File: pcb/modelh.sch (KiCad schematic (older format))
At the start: 39 parts, among them J1 USB_B, J2 Conn_01x16, J3 Conn_01x08, J4 Conn_01x04, J5 Conn_02x03_Odd_Even, J6 Conn_02x05_Odd_Even, SW1 SW_Push, U1 STM32F103C8Tx, U2 AMS1117-3.3, Y1 8MHz, Y2 32.768KHz

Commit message: Fix DRC
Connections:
- no-connect marks 2 -> 3
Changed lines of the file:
@@
 	1    0    0    -1
 $EndComp
-Text HLabel 9800 1950 0    50   Input ~ 0
-col7
-Text HLabel 9800 1850 0    50   Input ~ 0
-col6
-Text HLabel 9800 1750 0    50   Input ~ 0
-col5
-Text HLabel 9800 1650 0    50   Input ~ 0
-col4
-Text HLabel 9800 1550 0    50   Input ~ 0
-col3
-Text HLabel 9800 1450 0    50   Input ~ 0
-col2
-Text HLabel 9800 1350 0    50   Input ~ 0
-col1
-Text HLabel 9800 1250 0    50   Input ~ 0
-col0
 Wire Wire Line
 	10100 1250 9800 1250
@@
 Wire Wire Line
 	9800 1950 10100 1950
-Text HLabel 9800 2450 0    50   Input ~ 0
-col12
-Text HLabel 9800 2750 0    50   Input ~ 0
-col15
-Text HLabel 9800 2650 0    50   Input ~ 0
-col14
-Text HLabel 9800 2550 0    50   Input ~ 0
-col13
-Text HLabel 9800 2350 0    50   Input ~ 0
-col11
-Text HLabel 9800 2250 0    50   Input ~ 0
-col10
-Text HLabel 9800 2150 0    50   Input ~ 0
-col9
-Text HLabel 9800 2050 0    50   Input ~ 0
-col8
 Wire Wire Line
 	10100 2050 9800 2050
@@
 Wire Wire Line
 	9800 2750 10100 2750
-Text HLabel 9800 3900 0    50   Input ~ 0
-row7
-Text HLabel 9800 3800 0    50   Input ~ 0
-row6
-Text HLabel 9800 3700 0    50   Input ~ 0
-row5
-Text HLabel 9800 3600 0    50   Input ~ 0
-row4
-Text HLabel 9800 3500 0    50   Input ~ 0
-row3
-Text HLabel 9800 3400 0    50   Input ~ 0
-row2
-Text HLabel 9800 3300 0    50   Input ~ 0
-row1
-Text HLabel 9800 3200 0    50   Input ~ 0
-row0
 Wire Wire Line
 	10100 3200 9800 3200
@@
 	0    1    1    0
 $EndComp
-Text HLabel 9200 4750 0    50   Input ~ 0
-led2
-Text HLabel 9200 4550 0    50   Input ~ 0
-led1
-Text HLabel 9200 4450 0    50   Input ~ 0
-led0
 Wire Wire Line
 	9200 4450 9500 4450
@@
 Wire Wire Line
 	2250 1100 2250 1000
-Text HLabel 2350 1400 2    50   Input ~ 0
-D-
-Text HLabel 2350 1300 2    50   Input ~ 0
-D+
 $Comp
 L Device:R R3
@@
 	1    0    0    -1
 $EndComp
-Text HLabel 4800 4600 0    50   Input ~ 0
-col7
-Text HLabel 4800 4700 0    50   Input ~ 0
-col6
 Wire Wire Line
 	5100 4700 4800 4700
 Wire Wire Line
 	4800 4600 5100 4600
-Text HLabel 6700 4100 2    50   Input ~ 0
-col12
-Text HLabel 6700 3800 2    50   Input ~ 0
-col15
-Text HLabel 6700 3900 2    50   Input ~ 0
-col14
-Text HLabel 6700 4000 2    50   Input ~ 0
-col13
-Text HLabel 6700 4200 2    50   Input ~ 0
-col11
-Text HLabel 4800 3500 0    50   Input ~ 0
-col10
-Text HLabel 4800 3600 0    50   Input ~ 0
-col9
-Text HLabel 4800 4500 0    50   Input ~ 0
-col8
 Wire Wire Line
 	5100 4500 4800 4500
@@
 Wire Wire Line
 	6700 3800 6400 3800
-Text HLabel 4800 4100 0    50   Input ~ 0
-row0
 Wire Wire Line
 	5100 4100 4800 4100
-Text HLabel 4800 3300 0    50   Input ~ 0
-OSC32OUT
-Text HLabel 4800 3200 0    50   Input ~ 0
-OSC32IN
-Text HLabel 4800 2900 0    50   Input ~ 0
-OSC8OUT
-Text HLabel 4800 2800 0    50   Input ~ 0
-OSC8IN
 Wire Wire Line
 	5100 2800 4800 2800
@@
 Wire Wire Line
 	5100 2400 4800 2400
-Text HLabel 4150 6800 2    50   Input ~ 0
-nRST
 Wire Wire Line
 	4150 6800 3850 6800
@@
 	5550 7500 5650 7500
 Connection ~ 5650 7500
-Text HLabel 6300 6750 2    50   Input ~ 0
-OSC8OUT
-Text HLabel 6300 6450 2    50   Input ~ 0
-OSC8IN
 $Comp
 L Device:R R6
@@
 	6100 6750 5650 6750
 Connection ~ 5650 6750
-Text HLabel 6050 7500 2    50   Input ~ 0
-OSC32OUT
-Text HLabel 6050 7200 2    50   Input ~ 0
-OSC32IN
 Wire Wire Line
 	5650 7200 6050 7200
@@
 Wire Wire Line
 	5100 3900 4800 3900
-Text HLabel 4800 3900 0    50   Input ~ 0
-row2
-Text HLabel 6700 5000 2    50   Input ~ 0
-row3
-Text HLabel 4800 3800 0    50   Input ~ 0
-row4
 Wire Wire Line
 	6700 4900 6400 4900
 Wire Wire Line
 	6400 4800 6700 4800
-Text HLabel 6700 4800 2    50   Input ~ 0
-SWDIO
-Text HLabel 6700 4900 2    50   Input ~ 0
-SWCLK
 $Comp
 L power:GND #PWR0107
@@
 Wire Wire Line
 	1450 6450 1450 6350
-Text HLabel 4800 3100 0    50   Input ~ 0
-STATUSLED
 Wire Wire Line
 	5100 3100 4800 3100
-Text HLabel 1450 6350 1    50   Input ~ 0
-STATUSLED
 $Comp
 L power:+3.3V #PWR0108
@@
 	1    0    0    -1
 $EndComp
-Text HLabel 4800 2400 0    50   Input ~ 0
-nRST
 $Comp
 L Regulator_Linear:AMS1117-3.3 U2
@@
 Wire Wire Line
 	5100 2600 4800 2600
-Text HLabel 4800 2600 0    50   Input ~ 0
-BOOT0
 $Comp
 L power:GND #PWR0115
@@
 	5900 5300 5800 5300
 Connection ~ 5800 5300
-Text HLabel 6700 4600 2    50   Input ~ 0
-D-
-Text HLabel 6700 4700 2    50   Input ~ 0
-D+
 Wire Wire Line
 	6700 4600 6400 4600
@@
 Wire Wire Line
 	1550 5150 1250 5150
-Text HLabel 1250 5150 0    50   Input ~ 0
-BOOT0
 $Comp
 L power:+3.3V #PWR0116
@@
 Wire Wire Line
 	7700 1300 8000 1300
-Text HLabel 8000 1300 2    50   Input ~ 0
-SWDIO
-Text HLabel 8000 1400 2    50   Input ~ 0
-SWCLK
 Wire Wire Line
 	7700 1700 8000 1700
-Text HLabel 8000 1700 2    50   Input ~ 0
-nRST
 $Comp
 L Device:C C10
@@
 Wire Wire Line
 	6400 4500 6700 4500
-Text HLabel 6700 4500 2    50   Input ~ 0
-col0
-Text HLabel 6700 4400 2    50   Input ~ 0
-col1
-Text HLabel 6700 4300 2    50   Input ~ 0
-col2
-Text HLabel 4800 5000 0    50   Input ~ 0
-col3
-Text HLabel 4800 4900 0    50   Input ~ 0
-col4
-Text HLabel 4800 4800 0    50   Input ~ 0
-col5
 Wire Wire Line
 	4800 4400 5100 4400
@@
 Wire Wire Line
 	4800 4200 5100 4200
-Text HLabel 4800 4200 0    50   Input ~ 0
-led0
-Text HLabel 4800 4300 0    50   Input ~ 0
-led1
-Text HLabel 4800 4400 0    50   Input ~ 0
-led2
-Text HLabel 6700 3600 2    50   Input ~ 0
-row7
-Text HLabel 6700 3700 2    50   Input ~ 0
-row6
-Text HLabel 6700 3500 2    50   Input ~ 0
-row5
 Wire Wire Line
 	6700 3500 6400 3500
@@
 Wire Wire Line
 	2900 5150 3200 5150
-Text HLabel 3200 5150 2    50   Input ~ 0
+Wire Wire Line
+	5100 3700 4800 3700
+Wire Wire Line
+	4800 4000 5100 4000
+Text GLabel 9800 1250 0    50   Input ~ 0
+col0
+Text GLabel 9800 1350 0    50   Input ~ 0
+col1
+Text GLabel 9800 1450 0    50   Input ~ 0
+col2
+Text GLabel 9800 1550 0    50   Input ~ 0
+col3
+Text GLabel 9800 1650 0    50   Input ~ 0
+col4
+Text GLabel 9800 1750 0    50   Input ~ 0
+col5
+Text GLabel 9800 1850 0    50   Input ~ 0
+col6
+Text GLabel 9800 1950 0    50   Input ~ 0
+col7
+Text GLabel 9800 2050 0    50   Input ~ 0
+col8
+Text GLabel 9800 2150 0    50   Input ~ 0
+col9
+Text GLabel 9800 2250 0    50   Input ~ 0
+col10
+Text GLabel 9800 2350 0    50   Input ~ 0
+col11
+Text GLabel 9800 2450 0    50   Input ~ 0
+col12
+Text GLabel 9800 2550 0    50   Input ~ 0
+col13
+Text GLabel 9800 2650 0    50   Input ~ 0
+col14
+Text GLabel 9800 2750 0    50   Input ~ 0
+col15
+Text GLabel 9800 3200 0    50   Input ~ 0
+row0
+Text GLabel 9800 3300 0    50   Input ~ 0
+row1
+Text GLabel 9800 3400 0    50   Input ~ 0
+row2
+Text GLabel 9800 3500 0    50   Input ~ 0
+row3
+Text GLabel 9800 3600 0    50   Input ~ 0
+row4
+Text GLabel 9800 3700 0    50   Input ~ 0
+row5
+Text GLabel 9800 3800 0    50   Input ~ 0
+row6
+Text GLabel 9800 3900 0    50   Input ~ 0
+row7
+Text GLabel 9200 4450 0    50   Input ~ 0
+led0
+Text GLabel 9200 4550 0    50   Input ~ 0
+led1
+Text GLabel 9200 4750 0    50   Input ~ 0
+led2
+Text GLabel 2350 1300 2    50   Input ~ 0
+D+
+Text GLabel 2350 1400 2    50   Input ~ 0
+D-
+Text GLabel 1250 5150 0    50   Input ~ 0
+BOOT0
+Text GLabel 3200 5150 2    50   Input ~ 0
 BOOT1
-Wire Wire Line
-	5100 3700 4800 3700
-Text HLabel 4800 3700 0    50   Input ~ 0
+Text GLabel 1450 6350 1    50   Input ~ 0
+STATUSLED
+Text GLabel 4150 6800 2    50   Input ~ 0
+nRST
+Text GLabel 6050 7500 2    50   Input ~ 0
+OSC32OUT
+Text GLabel 6050 7200 2    50   Input ~ 0
+OSC32IN
+Text GLabel 6300 6750 2    50   Input ~ 0
+OSC8OUT
+Text GLabel 6300 6450 2    50   Input ~ 0
+OSC8IN
+Text GLabel 6700 3500 2    50   Input ~ 0
+row5
+Text GLabel 6700 3600 2    50   Input ~ 0
+row7
+Text GLabel 6700 3700 2    50   Input ~ 0
+row6
+Text GLabel 6700 3800 2    50   Input ~ 0
+col15
+Text GLabel 6700 3900 2    50   Input ~ 0
+col14
+Text GLabel 6700 4000 2    50   Input ~ 0
+col13
+Text GLabel 6700 4100 2    50   Input ~ 0
+col12
+Text GLabel 6700 4200 2    50   Input ~ 0
+col11
+Text GLabel 6700 4300 2    50   Input ~ 0
+col2
+Text GLabel 6700 4400 2    50   Input ~ 0
+col1
+Text GLabel 6700 4500 2    50   Input ~ 0
+col0
+Text GLabel 6700 4600 2    50   Input ~ 0
+D-
+Text GLabel 6700 4700 2    50   Input ~ 0
+D+
+Text GLabel 6700 4800 2    50   Input ~ 0
+SWDIO
+Text GLabel 6700 4900 2    50   Input ~ 0
+SWCLK
+Text GLabel 6700 5000 2    50   Input ~ 0
+row3
+Text GLabel 8000 1300 2    50   Input ~ 0
+SWDIO
+Text GLabel 8000 1400 2    50   Input ~ 0
+SWCLK
+Text GLabel 8000 1700 2    50   Input ~ 0
+nRST
+Text GLabel 4800 2400 0    50   Input ~ 0
+nRST
+Text GLabel 4800 2600 0    50   Input ~ 0
+BOOT0
+Text GLabel 4800 2800 0    50   Input ~ 0
+OSC8IN
+Text GLabel 4800 2900 0    50   Input ~ 0
+OSC8OUT
+Text GLabel 4800 3100 0    50   Input ~ 0
+STATUSLED
+Text GLabel 4800 3200 0    50   Input ~ 0
+OSC32IN
+Text GLabel 4800 3300 0    50   Input ~ 0
+OSC32OUT
+Text GLabel 4800 3500 0    50   Input ~ 0
+col10
+Text GLabel 4800 3600 0    50   Input ~ 0
+col9
+Text GLabel 4800 3700 0    50   Input ~ 0
 BOOT1
-Text HLabel 4800 4000 0    50   Input ~ 0
+Text GLabel 4800 3800 0    50   Input ~ 0
+row4
+Text GLabel 4800 3900 0    50   Input ~ 0
+row2
+Text GLabel 4800 4000 0    50   Input ~ 0
 row1
-Wire Wire Line
-	4800 4000 5100 4000
+Text GLabel 4800 4100 0    50   Input ~ 0
+row0
+Text GLabel 4800 4200 0    50   Input ~ 0
+led0
+Text GLabel 4800 4300 0    50   Input ~ 0
+led1
+Text GLabel 4800 4400 0    50   Input ~ 0
+led2
+Text GLabel 4800 4500 0    50   Input ~ 0
+col8
+Text GLabel 4800 4600 0    50   Input ~ 0
+col7
+Text GLabel 4800 4700 0    50   Input ~ 0
+col6
+Text GLabel 4800 4800 0    50   Input ~ 0
+col5
+Text GLabel 4800 4900 0    50   Input ~ 0
+col4
+Text GLabel 4800 5000 0    50   Input ~ 0
+col3
+NoConn ~ 7700 1500
 $EndSCHEMATC

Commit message: WIP
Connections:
- net led0: now also U1.46 (PB9); no longer U1.43 (PB7)
- net led2: now also U1.43 (PB7); no longer U1.46 (PB9)
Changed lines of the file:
@@
 	6400 4500 6700 4500
 Wire Wire Line
+	4800 4200 5100 4200
+Wire Wire Line
+	5100 4300 4800 4300
+Wire Wire Line
 	4800 4400 5100 4400
-Wire Wire Line
-	5100 4300 4800 4300
-Wire Wire Line
-	4800 4200 5100 4200
 Wire Wire Line
 	6700 3500 6400 3500
@@
 Text GLabel 4800 4100 0    50   Input ~ 0
 row0
-Text GLabel 4800 4200 0    50   Input ~ 0
+Text GLabel 4800 4400 0    50   Input ~ 0
 led0
 Text GLabel 4800 4300 0    50   Input ~ 0
 led1
-Text GLabel 4800 4400 0    50   Input ~ 0
+Text GLabel 4800 4200 0    50   Input ~ 0
 led2
 Text GLabel 4800 4500 0    50   Input ~ 0

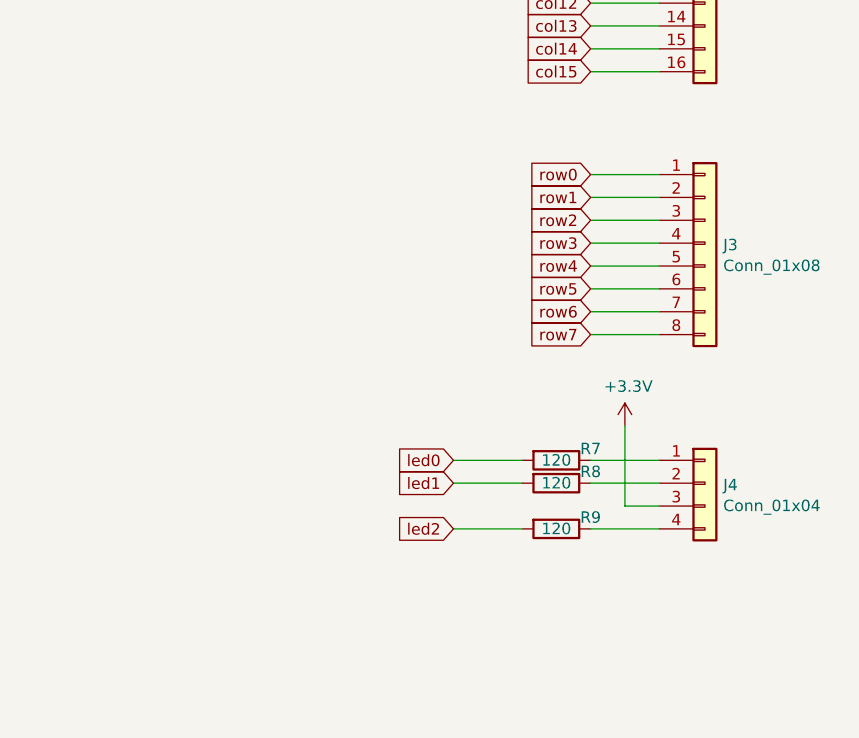
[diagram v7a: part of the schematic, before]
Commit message: Attempt at supporting 12 pin keyboards
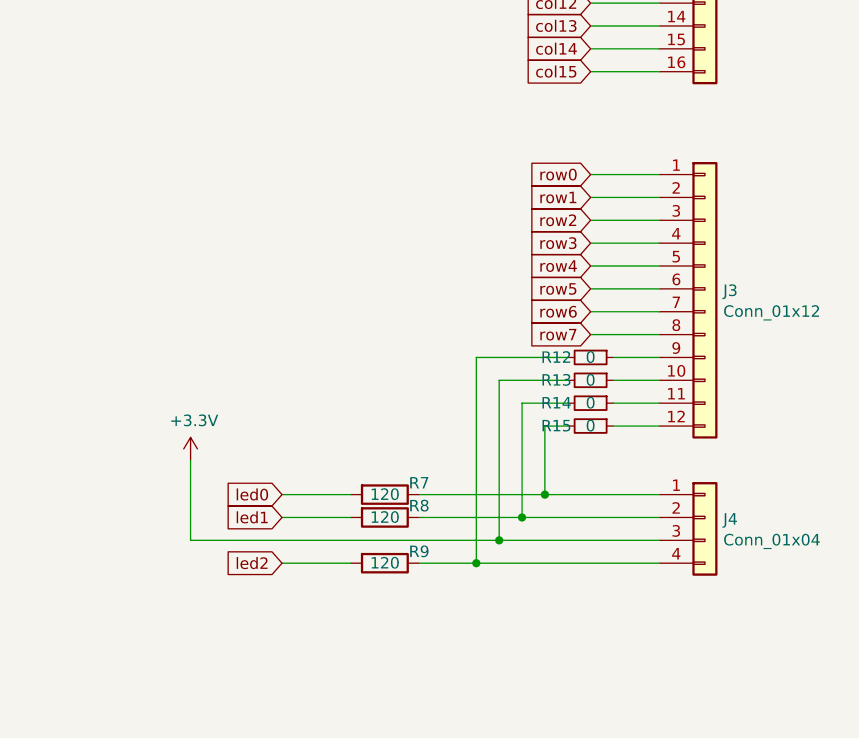
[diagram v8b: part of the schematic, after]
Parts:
- removed J3: Conn_01x08, Connector_PinHeader_2.54mm:PinHeader_1x08_P2.54mm_Vertical, symbol Connector_Generic:Conn_01x08
- added J3: Conn_01x12, Connector_PinSocket_2.54mm:PinSocket_1x12_P2.54mm_Vertical, symbol Connector_Generic:Conn_01x12
- added R12, R13, R14, R15: 0, Resistor_SMD:R_0805_2012Metric_Pad1.15x1.40mm_HandSolder, symbol Device:R_Small
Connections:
- net +3V3: now also R13.2
- net row0: now also J3.1 (Pin_1)
- net row1: now also J3.2 (Pin_2)
- net row2: now also J3.3 (Pin_3)
- net row3: now also J3.4 (Pin_4)
- net row4: now also J3.5 (Pin_5)
- net row5: now also J3.6 (Pin_6)
- net row6: now also J3.7 (Pin_7)
- net row7: now also J3.8 (Pin_8)
- net at J4.1 (Pin_1), R7.1: now also R15.2
- net at J4.2 (Pin_2), R8.1: now also R14.2
- net at J4.4 (Pin_4), R9.1: now also R12.2
- new net: J3.10 (Pin_10), R13.1
- new net: J3.11 (Pin_11), R14.1
- new net: J3.12 (Pin_12), R15.1
- new net: J3.9 (Pin_9), R12.1
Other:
- moved on the sheet: J4, R7, R8, R9
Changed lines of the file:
@@
-$EndComp
-$Comp
-L Connector_Generic:Conn_01x08 J3
-U 1 1 5E890C7F
-P 10300 3500
-F 0 "J3" H 10380 3492 50  0000 L CNN
-F 1 "Conn_01x08" H 10380 3401 50  0000 L CNN
-F 2 "Connector_PinHeader_2.54mm:PinHeader_1x08_P2.54mm_Vertical" H 10300 3500 50  0001 C CNN
-F 3 "~" H 10300 3500 50  0001 C CNN
-	1    10300 3500
-	1    0    0    -1
 $EndComp
 $Comp
 L Connector_Generic:Conn_01x04 J4
 U 1 1 5E891730
-P 10300 4550
-F 0 "J4" H 10380 4542 50  0000 L CNN
-F 1 "Conn_01x04" H 10380 4451 50  0000 L CNN
-F 2 "Connector_PinHeader_2.54mm:PinHeader_1x04_P2.54mm_Vertical" H 10300 4550 50  0001 C CNN
-F 3 "~" H 10300 4550 50  0001 C CNN
-	1    10300 4550
+P 10300 4700
+F 0 "J4" H 10380 4692 50  0000 L CNN
+F 1 "Conn_01x04" H 10380 4601 50  0000 L CNN
+F 2 "Connector_PinHeader_2.54mm:PinHeader_1x04_P2.54mm_Vertical" H 10300 4700 50  0001 C CNN
+F 3 "~" H 10300 4700 50  0001 C CNN
+	1    10300 4700
 	1    0    0    -1
 $EndComp
@@
 L Device:R R7
 U 1 1 5E91FFA8
-P 9650 4450
-F 0 "R7" V 9600 4600 50  0000 C CNN
-F 1 "120" V 9650 4450 50  0000 C CNN
-F 2 "Resistor_SMD:R_0603_1608Metric" V 9580 4450 50  0001 C CNN
-F 3 "~" H 9650 4450 50  0001 C CNN
-F 4 "C22787" H 9650 4450 50  0001 C CNN "LCSC"
-	1    9650 4450
+P 8900 4600
+F 0 "R7" V 8850 4750 50  0000 C CNN
+F 1 "120" V 8900 4600 50  0000 C CNN
+F 2 "Resistor_SMD:R_0603_1608Metric" V 8830 4600 50  0001 C CNN
+F 3 "~" H 8900 4600 50  0001 C CNN
+F 4 "C22787" H 8900 4600 50  0001 C CNN "LCSC"
+	1    8900 4600
 	0    1    1    0
 $EndComp
@@
 L Device:R R8
 U 1 1 5E920DCC
-P 9650 4550
-F 0 "R8" V 9600 4700 50  0000 C CNN
-F 1 "120" V 9650 4550 50  0000 C CNN
-F 2 "Resistor_SMD:R_0603_1608Metric" V 9580 4550 50  0001 C CNN
-F 3 "~" H 9650 4550 50  0001 C CNN
-F 4 "C22787" H 9650 4550 50  0001 C CNN "LCSC"
-	1    9650 4550
+P 8900 4700
+F 0 "R8" V 8850 4850 50  0000 C CNN
+F 1 "120" V 8900 4700 50  0000 C CNN
+F 2 "Resistor_SMD:R_0603_1608Metric" V 8830 4700 50  0001 C CNN
+F 3 "~" H 8900 4700 50  0001 C CNN
+F 4 "C22787" H 8900 4700 50  0001 C CNN "LCSC"
+	1    8900 4700
 	0    1    1    0
 $EndComp
@@
 L Device:R R9
 U 1 1 5E923217
-P 9650 4750
-F 0 "R9" V 9600 4900 50  0000 C CNN
-F 1 "120" V 9650 4750 50  0000 C CNN
-F 2 "Resistor_SMD:R_0603_1608Metric" V 9580 4750 50  0001 C CNN
-F 3 "~" H 9650 4750 50  0001 C CNN
-F 4 "C22787" H 9650 4750 50  0001 C CNN "LCSC"
-	1    9650 4750
-	0    1    1    0
-$EndComp
-Wire Wire Line
-	9200 4450 9500 4450
-Wire Wire Line
-	9500 4550 9200 4550
-Wire Wire Line
-	9200 4750 9500 4750
-Wire Wire Line
-	9800 4450 10100 4450
-Wire Wire Line
-	10100 4550 9800 4550
-Wire Wire Line
-	9800 4750 10100 4750
-Wire Wire Line
-	10100 4650 9950 4650
-Wire Wire Line
-	9950 4300 9950 4650
+P 8900 4900
+F 0 "R9" V 8850 5050 50  0000 C CNN
+F 1 "120" V 8900 4900 50  0000 C CNN
+F 2 "Resistor_SMD:R_0603_1608Metric" V 8830 4900 50  0001 C CNN
+F 3 "~" H 8900 4900 50  0001 C CNN
+F 4 "C22787" H 8900 4900 50  0001 C CNN "LCSC"
+	1    8900 4900
+	0    1    1    0
+$EndComp
+Wire Wire Line
+	8450 4600 8750 4600
+Wire Wire Line
+	8750 4700 8450 4700
+Wire Wire Line
+	8450 4900 8750 4900
+Wire Wire Line
+	8050 4450 8050 4800
 $Comp
 L Switch:SW_Push SW1
@@
 L power:+3.3V #PWR0111
 U 1 1 5F267CBD
-P 9950 4300
-F 0 "#PWR0111" H 9950 4150 50  0001 C CNN
-F 1 "+3.3V" H 9965 4473 50  0000 C CNN
-F 2 "" H 9950 4300 50  0001 C CNN
-F 3 "" H 9950 4300 50  0001 C CNN
-	1    9950 4300
+P 8050 4450
+F 0 "#PWR0111" H 8050 4300 50  0001 C CNN
+F 1 "+3.3V" H 8065 4623 50  0000 C CNN
+F 2 "" H 8050 4450 50  0001 C CNN
+F 3 "" H 8050 4450 50  0001 C CNN
+	1    8050 4450
 	1    0    0    -1
 $EndComp
@@
 Text GLabel 9800 3900 0    50   Input ~ 0
 row7
-Text GLabel 9200 4450 0    50   Input ~ 0
+Text GLabel 8450 4600 0    50   Input ~ 0
 led0
-Text GLabel 9200 4550 0    50   Input ~ 0
+Text GLabel 8450 4700 0    50   Input ~ 0
 led1
-Text GLabel 9200 4750 0    50   Input ~ 0
+Text GLabel 8450 4900 0    50   Input ~ 0
 led2
 Text GLabel 2350 1300 2    50   Input ~ 0
@@
 col3
 NoConn ~ 7700 1500
+$Comp
+L Connector_Generic:Conn_01x12 J3
+U 1 1 5F673091
+P 10300 3700
+F 0 "J3" H 10380 3692 50  0000 L CNN
+F 1 "Conn_01x12" H 10380 3601 50  0000 L CNN
+F 2 "Connector_PinSocket_2.54mm:PinSocket_1x12_P2.54mm_Vertical" H 10300 3700 50  0001 C CNN
+F 3 "~" H 10300 3700 50  0001 C CNN
+	1    10300 3700
+	1    0    0    -1
+$EndComp
+Wire Wire Line
+	9050 4600 9600 4600
+Wire Wire Line
+	9050 4700 9500 4700
+Wire Wire Line
+	8050 4800 9400 4800
+Wire Wire Line
+	9050 4900 9300 4900
+Wire Wire Line
+	9700 4100 9400 4100
+Wire Wire Line
+	9400 4100 9400 4800
+Connection ~ 9400 4800
+Wire Wire Line
+	9700 4000 9300 4000
+Wire Wire Line
+	9300 4000 9300 4900
+Connection ~ 9300 4900
+Wire Wire Line
+	9700 4200 9500 4200
+Wire Wire Line
+	9500 4200 9500 4700
+Connection ~ 9500 4700
+Wire Wire Line
+	9700 4300 9600 4300
+Wire Wire Line
+	9600 4300 9600 4600
+Connection ~ 9600 4600
+$Comp
+L Device:R_Small R12
+U 1 1 5F7A579E
+P 9800 4000
+F 0 "R12" V 9800 3850 50  0000 C CNN
+F 1 "0" V 9800 4000 50  0000 C CNN
+F 2 "Resistor_SMD:R_0805_2012Metric_Pad1.15x1.40mm_HandSolder" H 9800 4000 50  0001 C CNN
+F 3 "~" H 9800 4000 50  0001 C CNN
+	1    9800 4000
+	0    1    1    0
+$EndComp
+$Comp
+L Device:R_Small R13
+U 1 1 5F7D8C58
+P 9800 4100
+F 0 "R13" V 9800 3950 50  0000 C CNN
+F 1 "0" V 9800 4100 50  0000 C CNN
+F 2 "Resistor_SMD:R_0805_2012Metric_Pad1.15x1.40mm_HandSolder" H 9800 4100 50  0001 C CNN
+F 3 "~" H 9800 4100 50  0001 C CNN
+	1    9800 4100
+	0    1    1    0
+$EndComp
+$Comp
+L Device:R_Small R14
+U 1 1 5F7E51EA
+P 9800 4200
+F 0 "R14" V 9800 4050 50  0000 C CNN
+F 1 "0" V 9800 4200 50  0000 C CNN
+F 2 "Resistor_SMD:R_0805_2012Metric_Pad1.15x1.40mm_HandSolder" H 9800 4200 50  0001 C CNN
+F 3 "~" H 9800 4200 50  0001 C CNN
+	1    9800 4200
+	0    1    1    0
+$EndComp
+$Comp
+L Device:R_Small R15
+U 1 1 5F7F1728
+P 9800 4300
+F 0 "R15" V 9800 4150 50  0000 C CNN
+F 1 "0" V 9800 4300 50  0000 C CNN
+F 2 "Resistor_SMD:R_0805_2012Metric_Pad1.15x1.40mm_HandSolder" H 9800 4300 50  0001 C CNN
+F 3 "~" H 9800 4300 50  0001 C CNN
+	1    9800 4300
+	0    1    1    0
+$EndComp
+Wire Wire Line
+	9900 4100 10100 4100
+Wire Wire Line
+	10100 4200 9900 4200
+Wire Wire Line
+	9900 4300 10100 4300
+Wire Wire Line
+	9600 4600 10100 4600
+Wire Wire Line
+	9500 4700 10100 4700
+Wire Wire Line
+	9400 4800 10100 4800
+Wire Wire Line
+	9300 4900 10100 4900
+Wire Wire Line
+	10100 4000 9900 4000
 $EndSCHEMATC
